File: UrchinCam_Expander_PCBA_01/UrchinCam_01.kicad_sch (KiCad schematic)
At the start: 86 parts, among them J1 95157-440LF, J2 SM04B-GHS, J3 SM04B-GHS, J4 SM02B-GHS, J5 Conn_01x04_Pin, U1 MP6550, U2 ADS1115IDGS, U3 BNO085, U4 TSR3-2450N, U5 RTL8152B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

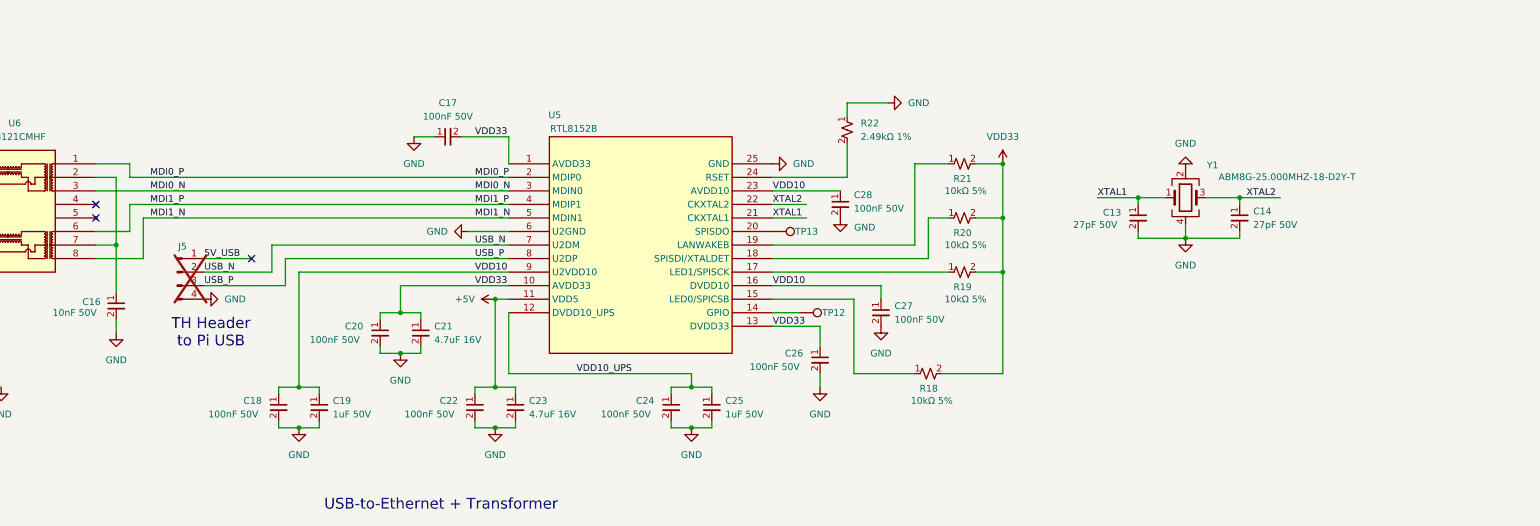
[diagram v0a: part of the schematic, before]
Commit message: Changed TH USB conn to JST.
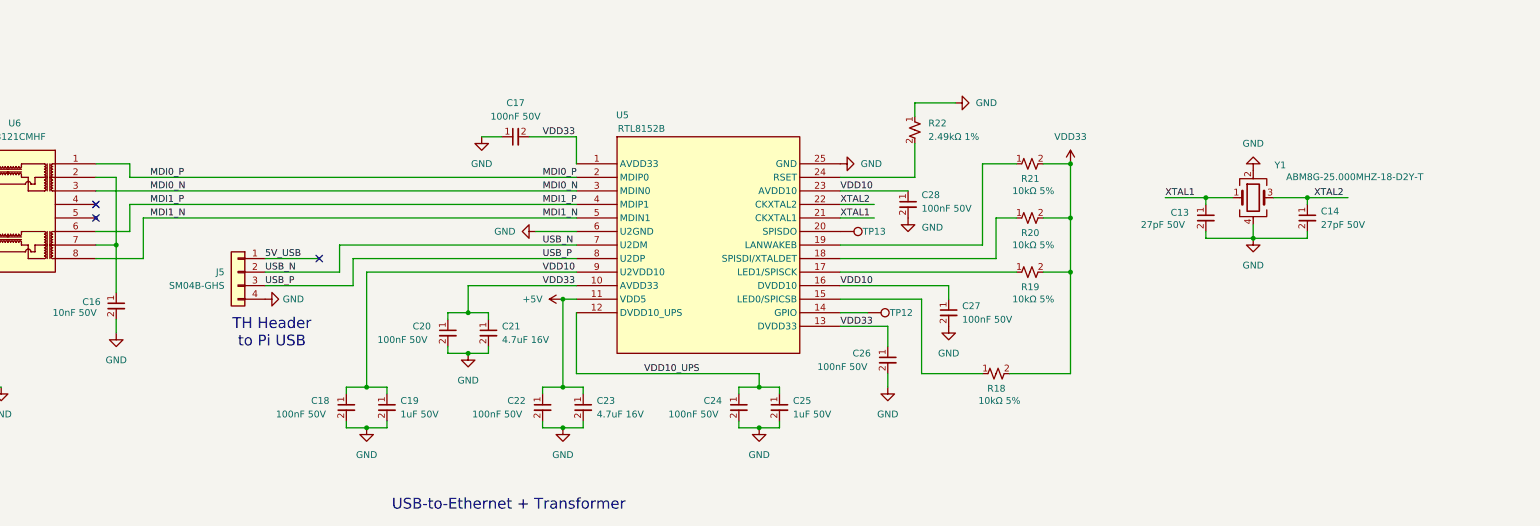
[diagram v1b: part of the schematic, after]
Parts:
- removed J5: Conn_01x04_Pin, Connector_PinHeader_2.54mm:PinHeader_1x04_P2.54mm_Vertical, symbol Connector:Conn_01x04_Pin
- added J5: SM04B-GHS, Connector_JST:JST_GH_SM04B-GHS-TB_1x04-1MP_P1.25mm_Horizontal, symbol Connectors:SM04B-GHS
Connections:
- net 5V_USB: now also J5.1 (Pin_1)
- net GND: now also J5.4 (Pin_4)
- net USB_N: now also J5.2 (Pin_2)
- net USB_P: now also J5.3 (Pin_3)
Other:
- moved on the sheet: C13, C14, C17, C18, C19, C20, C21, C22, C23, C24, C25, C26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

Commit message: Layout - placing tall components.
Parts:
- added C29: 10uF 50V, Capacitor_SMD:C_0805_2012Metric_Pad1.18x1.45mm_HandSolder, symbol Capacitors:CAP_10uF_0805_50V
- added C30: 10uF 10V, Capacitor_SMD:C_0402_1005Metric_Pad0.74x0.62mm_HandSolder, symbol Capacitors:CAP_10uF_0402_10V
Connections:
- net +5V: now also C30.1
- net GND: now also C29.2, C30.2
- net R+: now also J2.2 (Pin_2); no longer J2.3 (Pin_3)
- net R-: now also J2.1 (Pin_1); no longer J2.4 (Pin_4)
- net T+: now also J2.4 (Pin_4); no longer J2.1 (Pin_1)
- net T-: now also J2.3 (Pin_3); no longer J2.2 (Pin_2)
- net at C1.1, J4.1 (Pin_1), U4.1 (Vin): now also C29.1
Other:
- moved on the sheet: C5, C6, C7, C8, J2, J3, J4, R3, R4, R5, TP1, TP5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

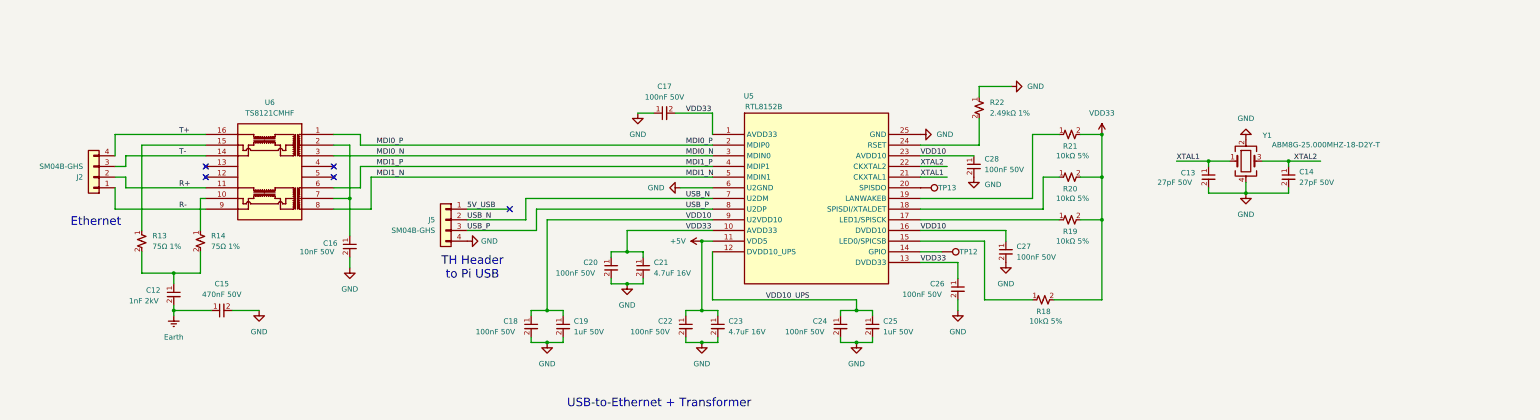
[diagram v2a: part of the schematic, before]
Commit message: Layout - routing ethernet + magnetics.
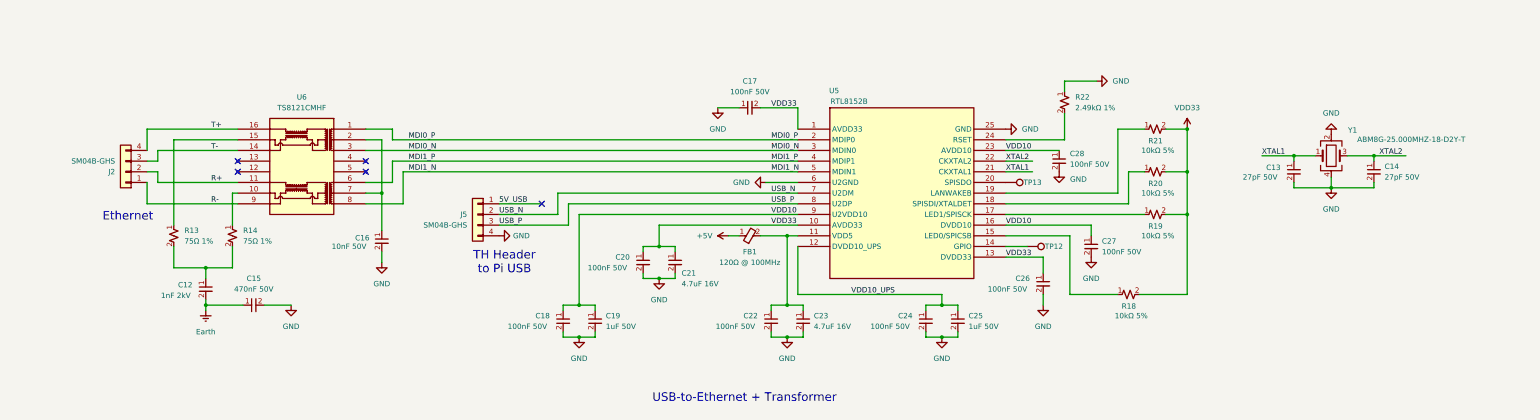
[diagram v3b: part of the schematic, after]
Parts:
- added FB1: 120Ω @ 100MHz, Resistor_SMD:R_0402_1005Metric_Pad0.72x0.64mm_HandSolder, symbol Ferrite_Beads:BLM15PD121SN1D
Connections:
- net +5V: now also FB1.1; no longer C22.1, C23.1, U5.11 (VDD5)
- new net: C22.1, C23.1, FB1.2, U5.11 (VDD5)
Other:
- moved on the sheet: C12, C13, C14, C15, C16, C17, C18, C19, C20, C21, C22, C23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

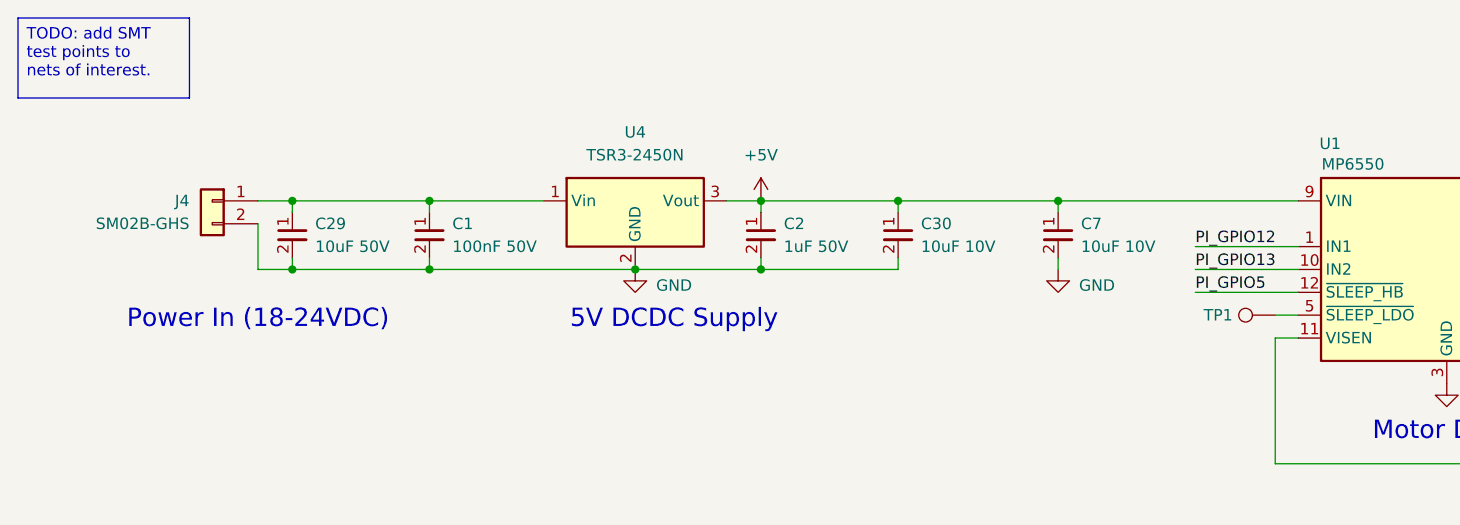
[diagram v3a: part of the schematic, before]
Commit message: All components except test points positioned.
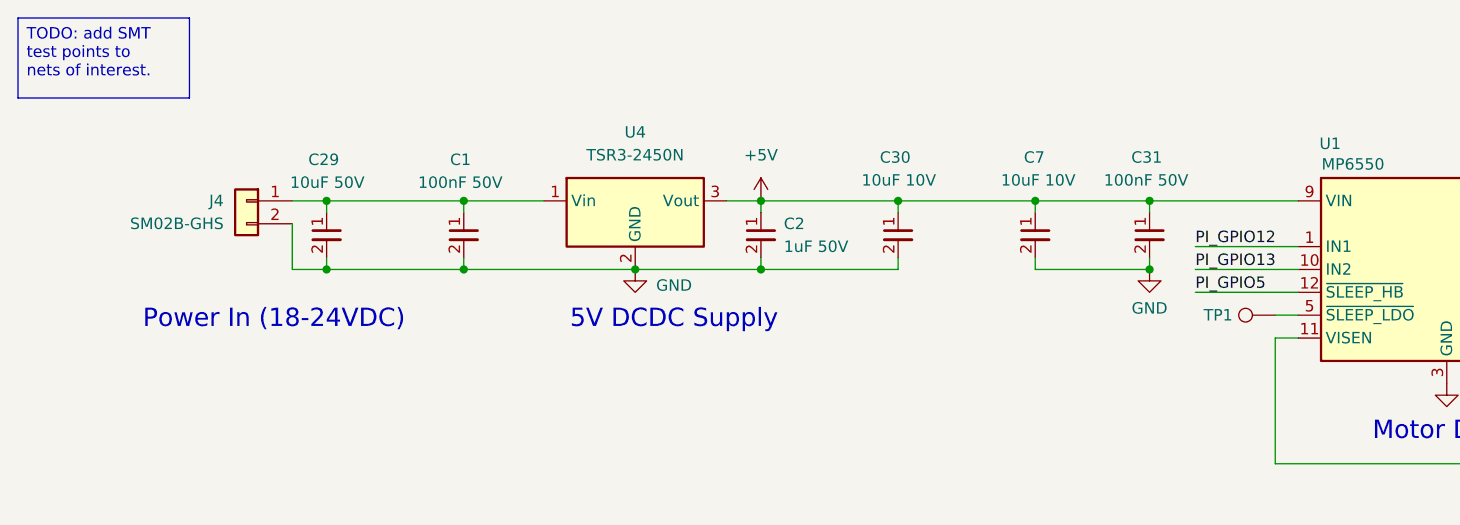
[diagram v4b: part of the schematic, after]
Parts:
- added C31: 100nF 50V, Capacitor_SMD:C_0402_1005Metric_Pad0.74x0.62mm_HandSolder, symbol Capacitors:CAP_100nF_0402_50V
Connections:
- net +5V: now also C31.1
- net GND: now also C31.2
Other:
- moved on the sheet: C1, C29, C7, J4

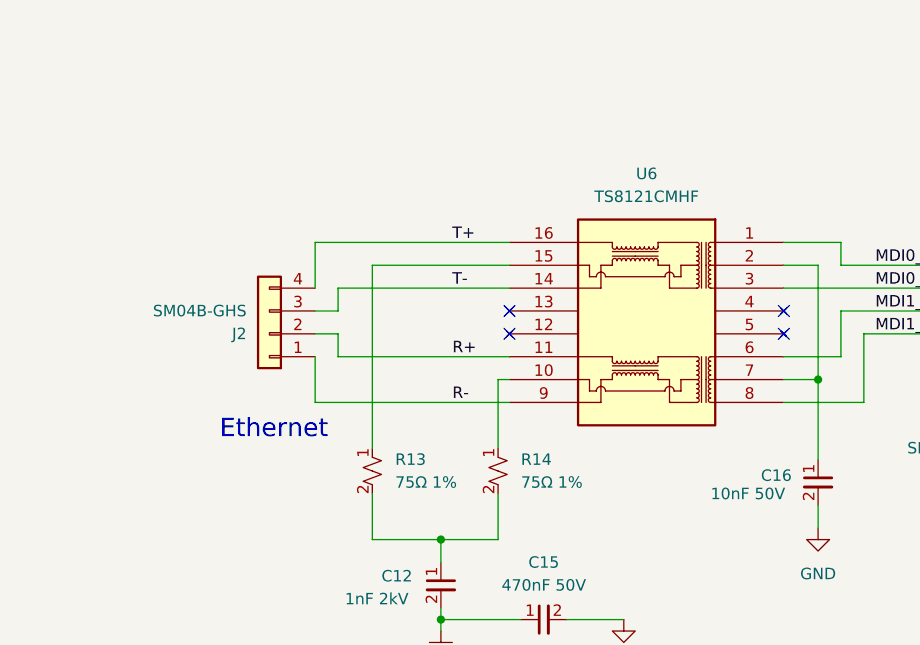
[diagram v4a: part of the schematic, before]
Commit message: Fixing ethernet routing.
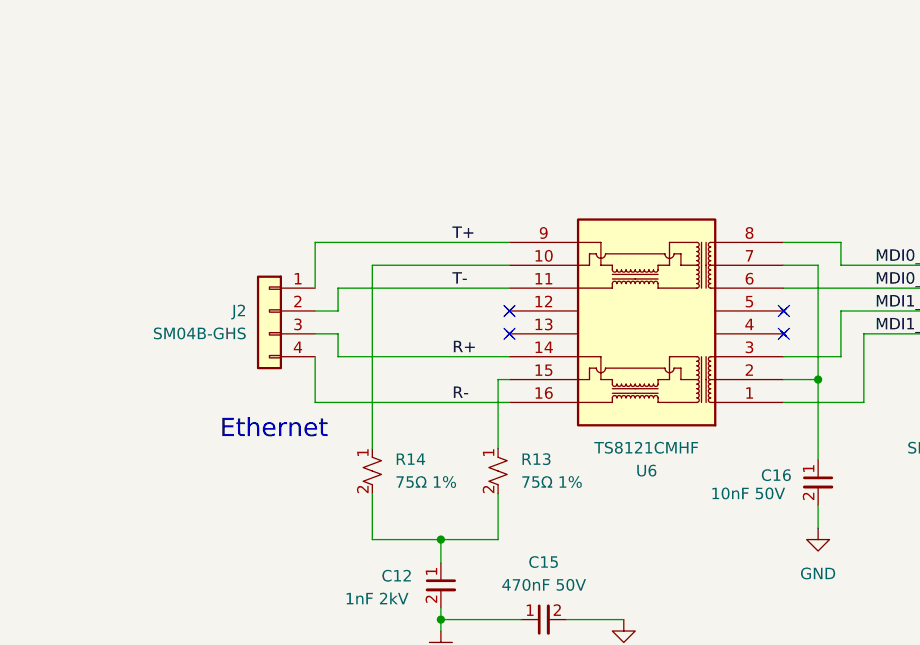
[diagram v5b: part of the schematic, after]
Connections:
- net MDI0_N: now also U6.6; no longer U6.3
- net MDI0_P: now also U6.8; no longer U6.1
- net MDI1_N: now also U6.1; no longer U6.8
- net MDI1_P: now also U6.3; no longer U6.6
- net R+: now also J2.3 (Pin_3), U6.14; no longer J2.2 (Pin_2), U6.11
- net R-: now also J2.4 (Pin_4), U6.16; no longer J2.1 (Pin_1), U6.9
- net T+: now also J2.1 (Pin_1), U6.9; no longer J2.4 (Pin_4), U6.16
- net T-: now also J2.2 (Pin_2), U6.11; no longer J2.3 (Pin_3), U6.14
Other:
- moved on the sheet: J2, R13, R14, U6
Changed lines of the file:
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@@
 	(wire
 		(pts
+			(xy 83.82 213.36) (xy 83.82 220.98)
+		)
+		(stroke
+			(width 0)
+			(type default)
+		)
+	)
+	(wire
+		(pts
 			(xy 283.21 223.52) (xy 267.97 223.52)
 		)
@@
 	(wire
 		(pts
-			(xy 83.82 226.06) (xy 83.82 231.14)
+			(xy 252.73 237.49) (xy 252.73 240.03)
 		)
 		(stroke
@@
 	(wire
 		(pts
-			(xy 252.73 237.49) (xy 252.73 240.03)
+			(xy 219.71 247.65) (xy 219.71 246.38)
 		)
 		(stroke
@@
 	(wire
 		(pts
-			(xy 219.71 247.65) (xy 219.71 246.38)
+			(xy 83.82 213.36) (xy 85.09 213.36)
 		)
 		(stroke
@@
 	(wire
 		(pts
-			(xy 83.82 213.36) (xy 85.09 213.36)
+			(xy 113.03 44.45) (xy 113.03 45.72)
 		)
 		(stroke
@@
 	(wire
 		(pts
-			(xy 113.03 44.45) (xy 113.03 45.72)
+			(xy 83.82 226.06) (xy 83.82 231.14)
 		)
 		(stroke
@@
 	(wire
 		(pts
+			(xy 69.85 200.66) (xy 69.85 220.98)
+		)
+		(stroke
+			(width 0)
+			(type default)
+		)
+	)
+	(wire
+		(pts
 			(xy 143.51 44.45) (xy 156.21 44.45)
 		)
@@
 	(wire
 		(pts
-			(xy 83.82 220.98) (xy 83.82 213.36)
-		)
-		(stroke
-			(width 0)
-			(type default)
-		)
-	)
-	(wire
-		(pts
 			(xy 181.61 232.41) (xy 181.61 233.68)
 		)
@@
 	(wire
 		(pts
-			(xy 69.85 226.06) (xy 69.85 231.14)
-		)
-		(stroke
-			(width 0)
-			(type default)
-		)
-	)
-	(wire
-		(pts
 			(xy 365.76 68.58) (xy 382.27 68.58)
 		)
@@
 	(wire
 		(pts
-			(xy 69.85 220.98) (xy 69.85 200.66)
-		)
-		(stroke
-			(width 0)
-			(type default)
-		)
-	)
-	(wire
-		(pts
 			(xy 111.76 114.3) (xy 113.03 114.3)
 		)
@@
 	(wire
 		(pts
+			(xy 69.85 226.06) (xy 69.85 231.14)
+		)
+		(stroke
+			(width 0)
+			(type default)
+		)
+	)
+	(wire
+		(pts
 			(xy 80.01 44.45) (xy 88.9 44.45)
 		)
@@
 	(symbol
 		(lib_id "Transformers:TS8121CMHF")
-		(at 100.33 207.01 0)
-		(mirror y)
+		(at 100.33 207.01 180)
 		(unit 1)
 		(exclude_from_sim no)
@@
 		(fields_autoplaced yes)
 		(property "Reference" "U6"
-			(at 100.33 190.5 0)
+			(at 100.33 223.52 0)
 			(effects
 				(font
@@
 		)
 		(property "Value" "TS8121CMHF"
-			(at 100.33 193.04 0)
+			(at 100.33 220.98 0)
 			(effects
 				(font
@@
 		)
 		(property "Description" "SMD 10/100 SINGLE PORT POE 15W"
-			(at 100.076 220.726 0)
+			(at 100.076 193.294 0)
 			(effects
 				(font
@@
 	(symbol
 		(lib_id "Resistors:Res_75R_0402_1p")
-		(at 83.82 223.52 0)
+		(at 69.85 223.52 0)
 		(unit 1)
 		(exclude_from_sim no)
@@
 		(fields_autoplaced yes)
 		(property "Reference" "R14"
-			(at 86.36 222.2499 0)
+			(at 72.39 222.2499 0)
 			(effects
 				(font
@@
 		)
 		(property "Value" "75Ω 1%"
-			(at 86.36 224.7899 0)
+			(at 72.39 224.7899 0)
 			(effects
 				(font
@@
 		)
 		(property "Footprint" "Resistor_SMD:R_0402_1005Metric_Pad0.72x0.64mm_HandSolder"
-			(at 85.09 236.474 0)
+			(at 71.12 236.474 0)
 			(effects
 				(font
@@
 		)
 		(property "Datasheet" ""
-			(at 83.82 223.52 0)
+			(at 69.85 223.52 0)
 			(effects
 				(font
@@
 		)
 		(property "Description" "RES 75 OHM 1% 1/16W 0402 p/n RC0402FR-0775RL"
-			(at 84.582 233.68 0)
+			(at 70.612 233.68 0)
 			(effects
 				(font
@@
 	(symbol
 		(lib_id "Connectors:SM04B-GHS")
-		(at 58.42 207.01 180)
+		(at 58.42 207.01 0)
+		(mirror y)
 		(unit 1)
 		(exclude_from_sim no)
@@
 		(fields_autoplaced yes)
 		(property "Reference" "J2"
-			(at 55.88 208.2801 0)
+			(at 55.88 205.7399 0)
 			(effects
 				(font
@@
 		)
 		(property "Value" "SM04B-GHS"
-			(at 55.88 205.7401 0)
+			(at 55.88 208.2799 0)
 			(effects
 				(font
@@
 		)
 		(property "Footprint" "Connector_JST:JST_GH_SM04B-GHS-TB_1x04-1MP_P1.25mm_Horizontal"
-			(at 57.912 195.072 0)
+			(at 57.912 218.948 0)
 			(effects
 				(font
@@
 		)
 		(property "Description" "CONN HEADER SMD R/A 4POS 1.25MM"
-			(at 56.896 197.612 0)
+			(at 56.896 216.408 0)
 			(effects
 				(font
@@
 	(symbol
 		(lib_id "Resistors:Res_75R_0402_1p")
-		(at 69.85 223.52 0)
+		(at 83.82 223.52 0)
 		(unit 1)
 		(exclude_from_sim no)
@@
 		(fields_autoplaced yes)
 		(property "Reference" "R13"
-			(at 72.39 222.2499 0)
+			(at 86.36 222.2499 0)
 			(effects
 				(font
@@
 		)
 		(property "Value" "75Ω 1%"
-			(at 72.39 224.7899 0)
+			(at 86.36 224.7899 0)
 			(effects
 				(font
@@
 		)
 		(property "Footprint" "Resistor_SMD:R_0402_1005Metric_Pad0.72x0.64mm_HandSolder"
-			(at 71.12 236.474 0)
+			(at 85.09 236.474 0)
 			(effects
 				(font
@@
 		)
 		(property "Datasheet" ""
-			(at 69.85 223.52 0)
+			(at 83.82 223.52 0)
 			(effects
 				(font
@@
 		)
 		(property "Description" "RES 75 OHM 1% 1/16W 0402 p/n RC0402FR-0775RL"
-			(at 70.612 233.68 0)
+			(at 84.582 233.68 0)
 			(effects
 				(font

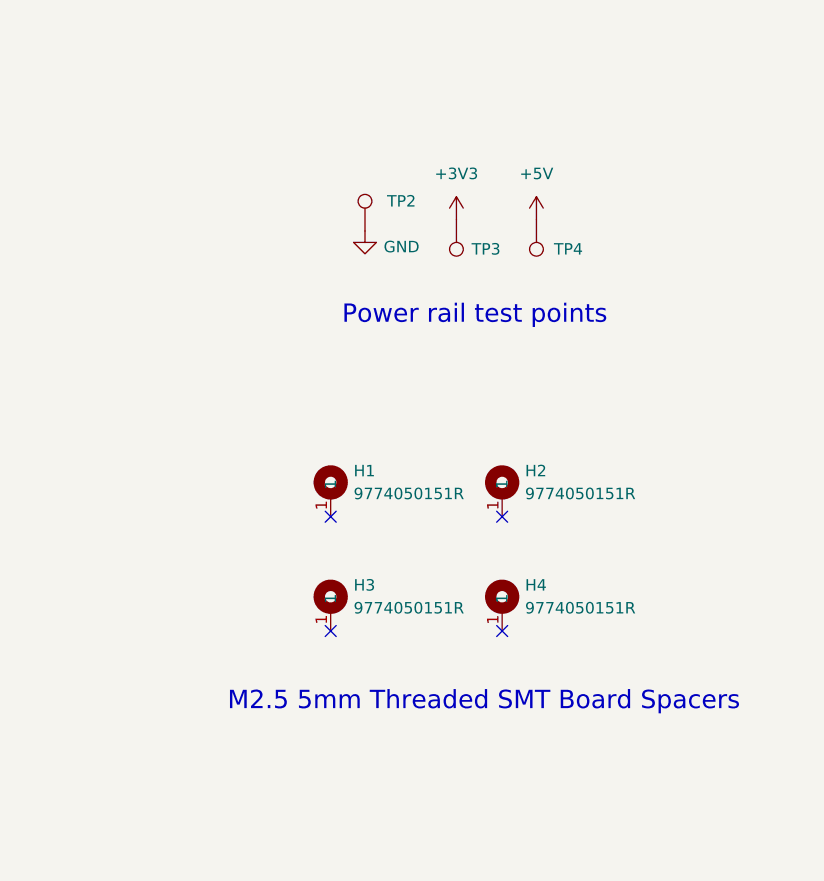
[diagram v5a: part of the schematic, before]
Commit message: Fixing via diameters.
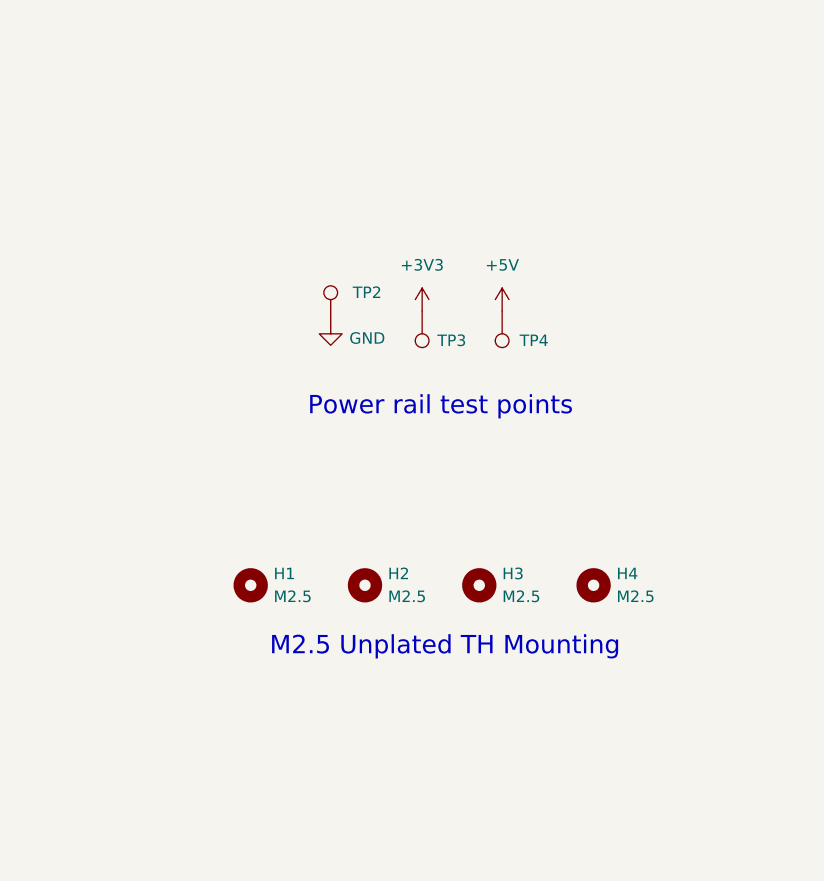
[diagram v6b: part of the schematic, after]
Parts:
- removed H1, H2, H3, H4: 9774050151R, Mounting_Wuerth:Mounting_Wuerth_WA-SMSI-M2.5_H5mm_9774050151R, symbol Board_Spacers:9774050151R
- added H1, H2, H3, H4: M2.5, Mounting_Holes:M2.5_Mounting_Hole_2.9mm_unplated, symbol Mounting_Holes:Mounting_Hole_M2.5
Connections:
- no-connect marks 29 -> 25
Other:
- note added: "M2.5 Unplated TH Mounting"
- note removed: "M2.5 5mm Threaded SMT Board Spacers"
- moved on the sheet: TP2, TP3, TP4
